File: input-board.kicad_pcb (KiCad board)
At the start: 2 copper layers, 70 parts, among them J1 BTNCON, J12 CAN, J2 BTNCON, J3 SWD, J7 I2C, J8 GAS, J9 BREMSE, SW1 switch-with-led, SW2 switch-with-led, SW3 switch-with-led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

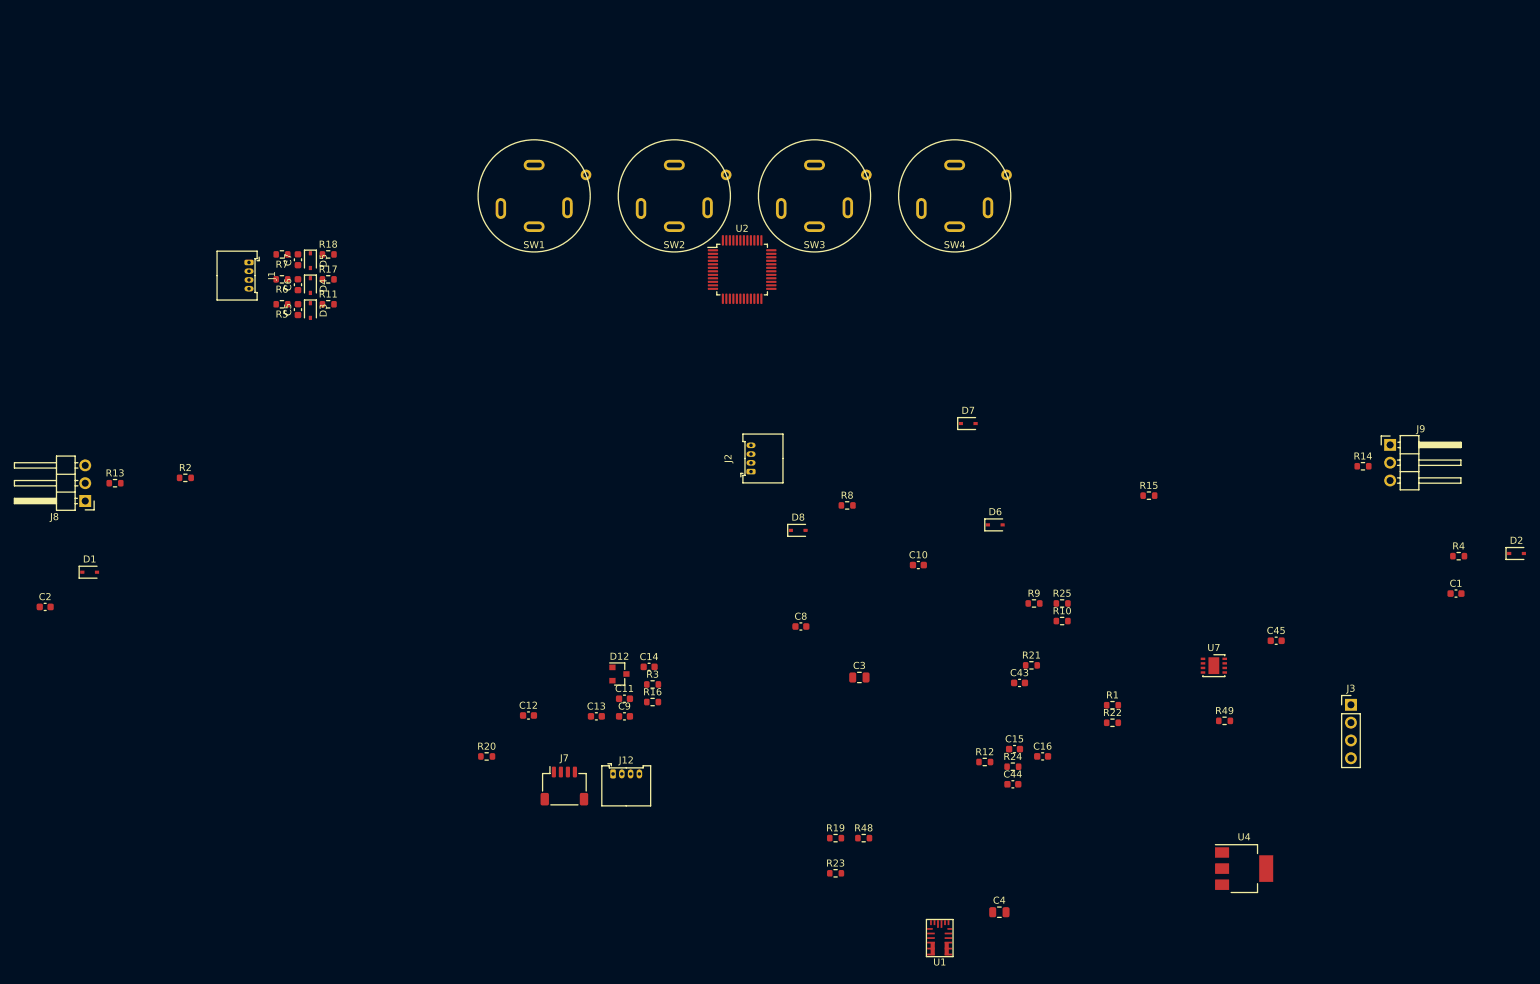
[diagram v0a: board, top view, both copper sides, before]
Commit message: organizing parts on layout
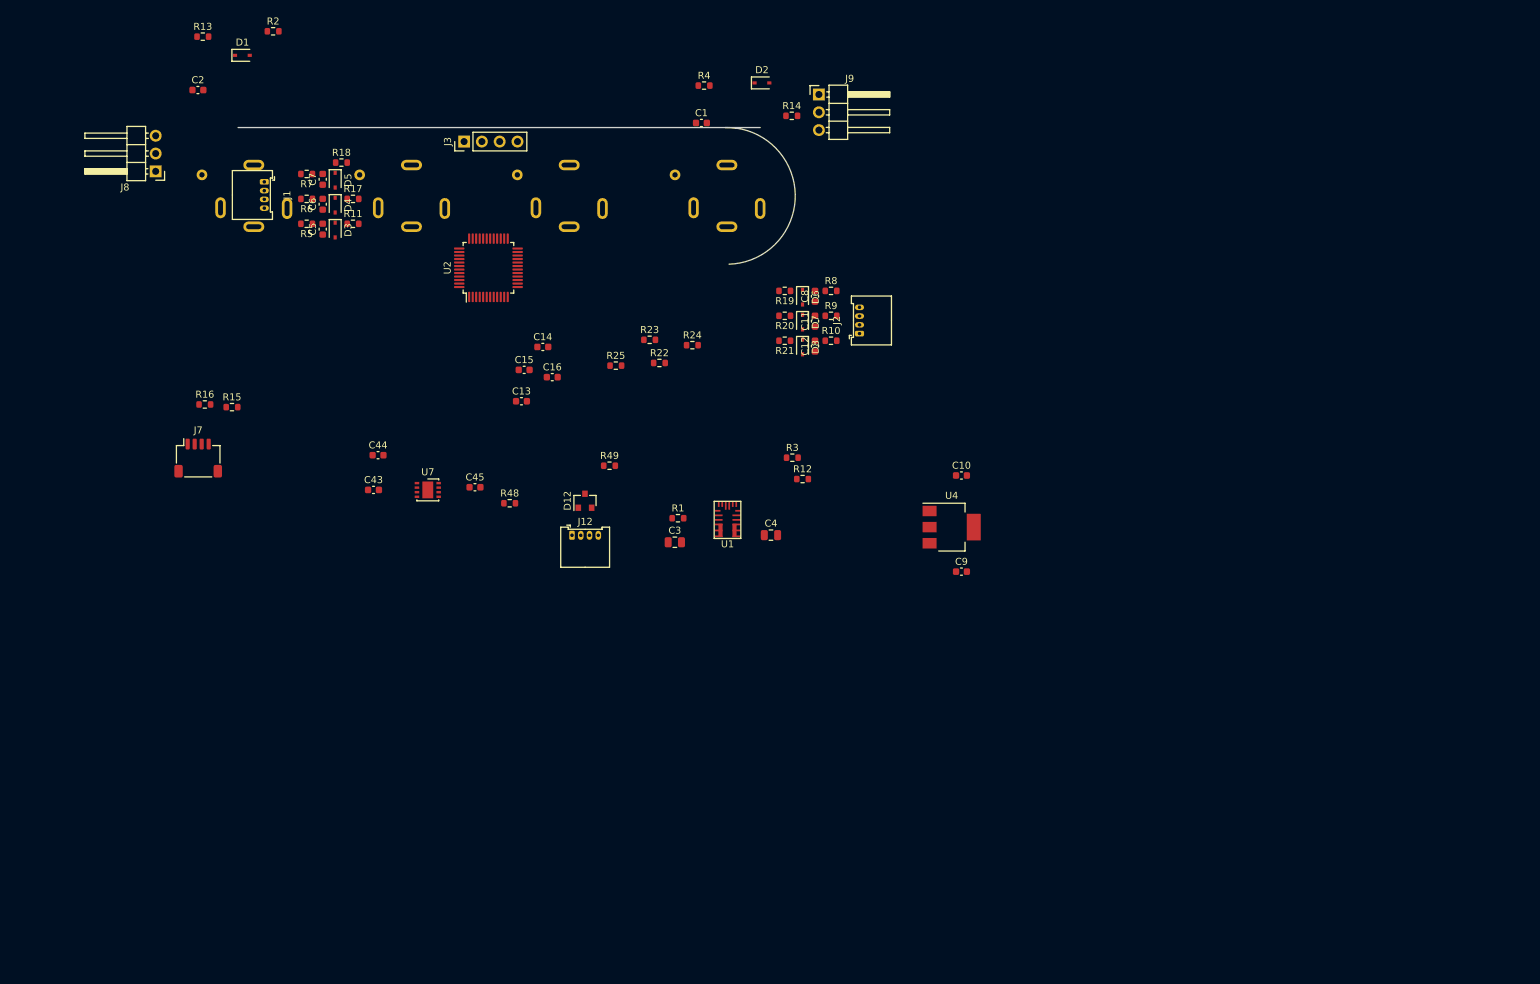
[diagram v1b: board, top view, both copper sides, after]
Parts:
- SW1, SW2, SW3, SW4: moved to B.Cu
- moved J3 149.9 mm to (130.0, 22.2), turned to 90 degrees
- moved R15 131.4 mm to (96.9, 60.1)
- moved C1 126.9 mm to (163.9, 19.6)
- moved D2 126.9 mm to (172.5, 13.9)
- moved R4 126.9 mm to (164.2, 14.3)
- moved C45 116.4 mm to (131.6, 71.6)
- moved U7 114.9 mm to (124.8, 72.0)
- moved C44 102.0 mm to (117.7, 67.0)
- moved C43 96.2 mm to (117.1, 72.0)
- moved R14 95.6 mm to (176.8, 18.6)
- moved J9 95.6 mm to (180.6, 15.5)
- moved R49 95.0 mm to (150.8, 68.5)
- moved C16 88.4 mm to (142.6, 55.9)
- moved C15 88.4 mm to (138.6, 54.8)
- moved R22 82.5 mm to (157.9, 53.8)
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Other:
- board outline added: 79.5 x 19.5 mm

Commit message: more component placing
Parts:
- moved R13 41.6 mm to (117.5, 40.8), turned to 180 degrees
- moved R24 38.1 mm to (124.8, 55.5)
- moved C2 36.4 mm to (120.0, 38.2), turned to 270 degrees
- moved D2 35.5 mm to (150.5, 41.8), turned to 270 degrees
- moved R2 35.4 mm to (118.5, 38.2), turned to 90 degrees
- moved J9 34.6 mm to (153.2, 36.8)
- moved R14 34.0 mm to (149.8, 39.2)
- moved D1 33.7 mm to (116.8, 38.2), turned to 90 degrees
- moved R22 33.6 mm to (124.2, 52.5)
- moved J8 32.6 mm to (114.0, 43.3)
- moved R4 31.6 mm to (148.8, 41.8), turned to 270 degrees
- moved C11 29.2 mm to (157.3, 29.6)
- moved R20 29.2 mm to (153.0, 28.9)
- moved R9 29.2 mm to (159.6, 28.9)
- moved C12 29.2 mm to (157.3, 33.2)
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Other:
- board size 79.5 x 19.5 mm -> 87.5 x 30 mm

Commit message: more layouting
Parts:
- added C17: 100n, Capacitor_SMD:C_0603_1608Metric, F.Cu at (138.8, 47.2)
- added X1: ASCO, Oscillator:Oscillator_SMD_Abracon_ASDMB-4Pin_2.5x2.0mm, F.Cu at (138.8, 45.0)
- moved C9 98.9 mm to (112.8, 39.0)
- moved C10 93.6 mm to (113.5, 36.5), turned to 270 degrees
- moved U4 90.0 mm to (118.8, 37.8)
- moved C43 48.3 mm to (148.8, 35.5)
- moved C44 45.8 mm to (152.8, 37.5), turned to 270 degrees
- moved C4 42.7 mm to (153.2, 41.0)
- moved U7 42.0 mm to (149.5, 38.0), turned to 180 degrees
- moved C3 37.4 mm to (149.8, 43.5), turned to 270 degrees
- moved R16 36.5 mm to (126.2, 44.8), turned to 270 degrees
- moved D12 36.3 mm to (145.0, 37.2)
- moved J7 35.8 mm to (120.0, 45.0)
- moved J12 35.5 mm to (143.0, 43.0)
- moved U1 35.3 mm to (153.8, 44.0), turned to 90 degrees
- moved C45 34.8 mm to (145.0, 39.5), turned to 180 degrees
- moved R48 33.6 mm to (143.5, 41.0)
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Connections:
- SW1 pad 1: GND -> MDBT1
- SW1 pad 2: MDBT1 -> GND
- SW2 pad 1: GND -> MDBT2
- SW2 pad 2: MDBT2 -> GND
- U2 pad 18: MDBT1 -> MDBT4
- U2 pad 19: MDLED1 -> MDLED4
- U2 pad 21: MDBT2 -> BTN6
- U2 pad 22: MDLED2 -> BTN5
- U2 pad 25: MDBT3 -> BTN4
- U2 pad 26: MDLED3 -> MDBT3
- U2 pad 27: MDBT4 -> MDLED3
- U2 pad 28: MDLED4 -> MDLED2
- U2 pad 29: (no net) -> MDBT2
- U2 pad 31: BTN3 -> (no net)
- U2 pad 38: BTN6 -> BTN3
- U2 pad 39: BTN1 -> BTN2
- U2 pad 40: BTN2 -> BTN1
- U2 pad 42: BTN4 -> MDLED1
- U2 pad 43: BTN5 -> MDBT1
- U2 pad 5: (no net) -> Net-(U2-Pad5)
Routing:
- net +3V3: track 0.00 -> 71.6 mm, vias 0 -> 4
- net +5V: track 0.00 -> 62.0 mm, vias 0 -> 2
- net MDLED4: track 0.00 -> 51.2 mm, vias 0 -> 2
- net MDLED1: track 0.00 -> 46.8 mm, vias 0 -> 2
- net BTN4: track 0.00 -> 33.8 mm, vias 0 -> 4
- net BTN3: track 0.00 -> 33.8 mm, vias 0 -> 4
- net MDBT4: track 0.00 -> 33.2 mm, vias 0 -> 2
- net BTN5: track 0.00 -> 32.8 mm, vias 0 -> 4
- net MDBT1: track 0.00 -> 32.2 mm, vias 0 -> 2
- net BTN1: track 0.00 -> 30.6 mm, vias 0 -> 2
- net BTN6: track 0.00 -> 30.2 mm, vias 0 -> 2
- net BTN2: track 0.00 -> 30.0 mm, vias 0 -> 4
- net CAN_TX: track 0.00 -> 22.7 mm, vias 0 -> 2
- net CAN_RX: track 0.00 -> 22.0 mm, vias 0 -> 2
- net MDLED2: track 0.00 -> 17.8 mm, vias 0 -> 1
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- added copper zone on B.Cu, net GND
- added copper zone on F.Cu, net GND
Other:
- board size 87.5 x 30 mm -> 87.5 x 28.2 mm
- net class Default: clearance 0.2 -> 0.15; trace_width 0.25 -> 0.15; via_dia 0.8 -> 0.5; via_drill 0.4 -> 0.2
- rule trace_clearance: 0.2 -> 0.15
- rule trace_min: 0.2 -> 0.15
- rule via_min_drill: 0.3 -> 0.2
- rule via_min_size: 0.4 -> 0.5
